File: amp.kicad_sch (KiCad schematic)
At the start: 76 parts, among them J1 Input a/b/M, J3 Speaker 8/6/4/0, P1 25k, P2 25k, P3 25k, P4 25k, T1 E-1220, T2 AP-634/2

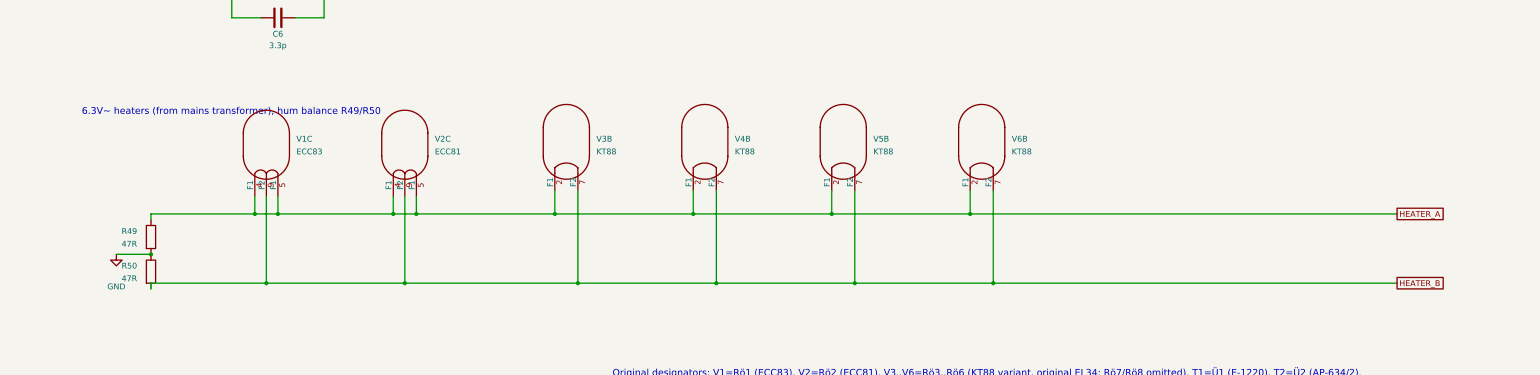
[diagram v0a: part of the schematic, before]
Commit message: KT88: 12.6V heaters, centre grounded at the tubes
- ECC83/ECC81 in 12.6V mode (pins 4-5), pin 9 to GND
- KT88 heaters in series strings V3+V4, V5+V6, midpoints to GND
- Remove hum-balance resistors R49/R50
- T101: custom transformer, 12.6V 4A heater winding (no CT),
  HV windings 310V 0.35A
- KT88.md updated

Co-Authored-By: Claude Opus 5.5 <noreply@anthropic.com>
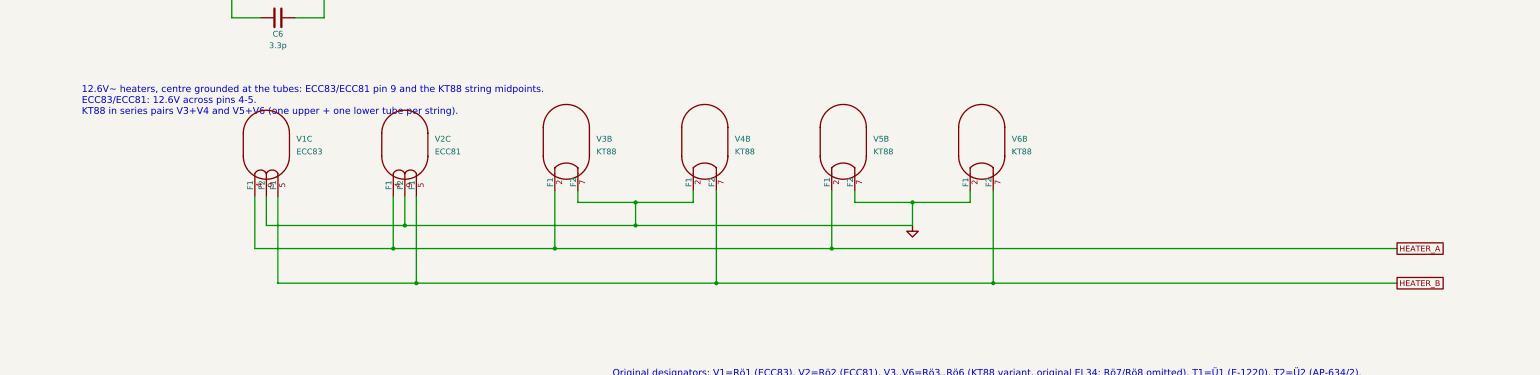
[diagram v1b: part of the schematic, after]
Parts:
- removed R49, R50: 47R, Resistor_THT:R_Axial_DIN0207_L6.3mm_D2.5mm_P10.16mm_Horizontal, symbol Device:R
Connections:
- net GND: now also V1.9 (F2), V2.9 (F2), V3.7 (F2), V4.2 (F1), V5.7 (F2), V6.2 (F1)
- net HEATER_A: no longer V1.5 (F1), V2.5 (F1), V4.2 (F1), V6.2 (F1)
- net HEATER_B: now also V1.5 (F1), V2.5 (F1); no longer V1.9 (F2), V2.9 (F2), V3.7 (F2), V5.7 (F2)
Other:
- note added: "12.6V~ heaters, centre grounded at the tubes: ECC83/ECC81 pin 9 and the KT88 string midpoints. ECC83/ECC81: 12.6V across pins 4-5. KT88 in series pairs V3+V4 and V5+V6 (one upper + one lower tube per string)."
- note removed: "6.3V~ heaters (from mains transformer), hum balance R49/R50"

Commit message: SMPS variant: draft schematic replacing the mains supply
Replace supply.kicad_sch with two sheets:
- smps_pri: mains input/EMI filter, NTC + relay bypass, UC3854B PFC
  (390 V bus), fixed-frequency LLC half-bridge (UCC25600 + UCC27714),
  current transformer, startup and aux supply, bus-OK logic.
- smps_sec: T201, both bank supplies (SiC bridge, CM choke, cap
  multiplier, 52 s B+ delay), heater buck synced from W3.

Net labels to the amp sheet are unchanged; D5/D6 become UF4007 for the
100 kHz bias windings. Adds T_SMPS_PPP and UC3854B symbols. Values are
start values; see SMPS.md for open points.

Co-Authored-By: Claude Opus 5.5 <noreply@anthropic.com>
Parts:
- D5, D6: value 1N4007 -> UF4007
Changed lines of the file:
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@@
 			)
 		)
-		(property "Value" "1N4007"
+		(property "Value" "UF4007"
 			(at 448.31 159.512 0)
 			(effects
@@
 			)
 		)
-		(property "Value" "1N4007"
+		(property "Value" "UF4007"
 			(at 448.31 186.436 0)
 			(effects
